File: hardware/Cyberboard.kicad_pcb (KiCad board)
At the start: 2 copper layers, 51 x 21 mm, 66 parts, among them CN1 B2B-XH-A (LF)(SN), J1 Conn_01x20, J2 Conn_01x20, SW1 SW_Push, SW2 SW_Push, U1 TPS630701RNMR, U2 NX2012SA-32.768KHZ-STD-MUB-2, U3 XL-1005UBC_C22355736, U4 STM32WB55RGVx, U5 BQ24074RGT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

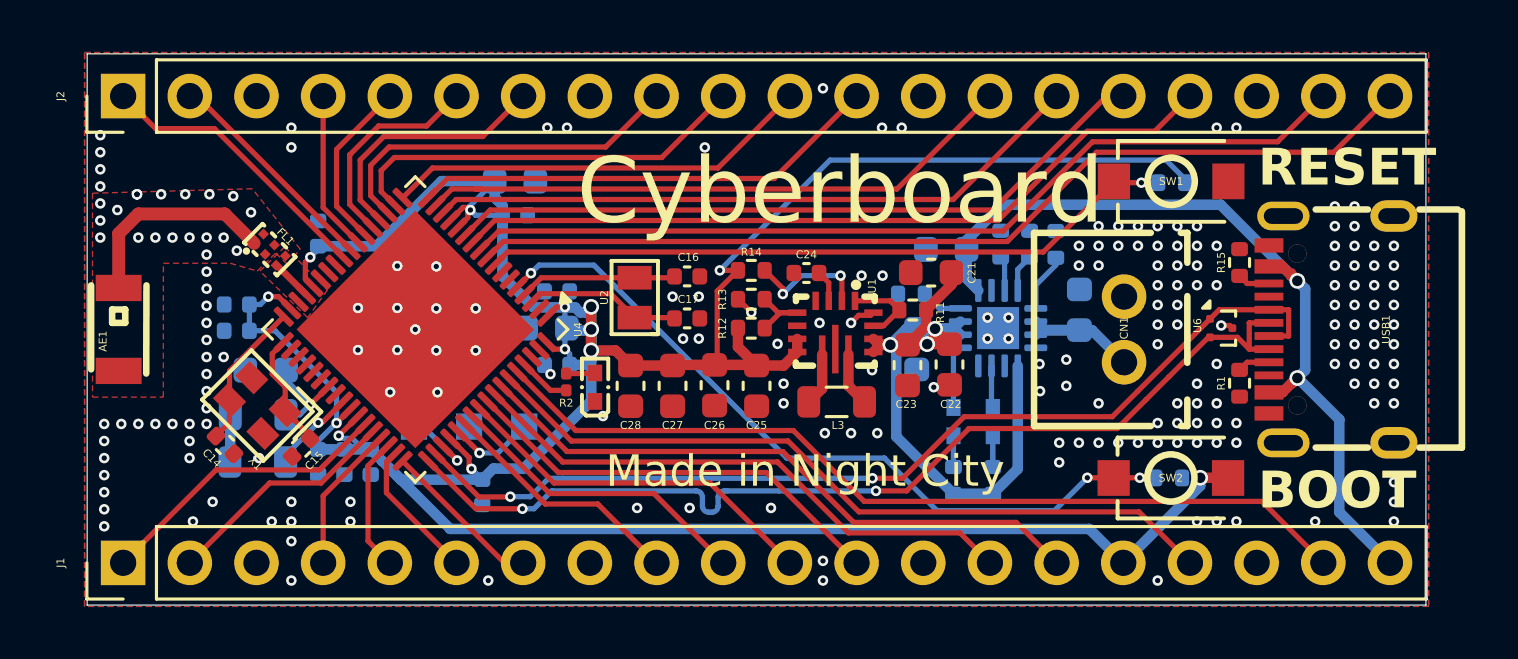
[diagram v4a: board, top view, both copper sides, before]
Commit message: updated pcb for single side pcba
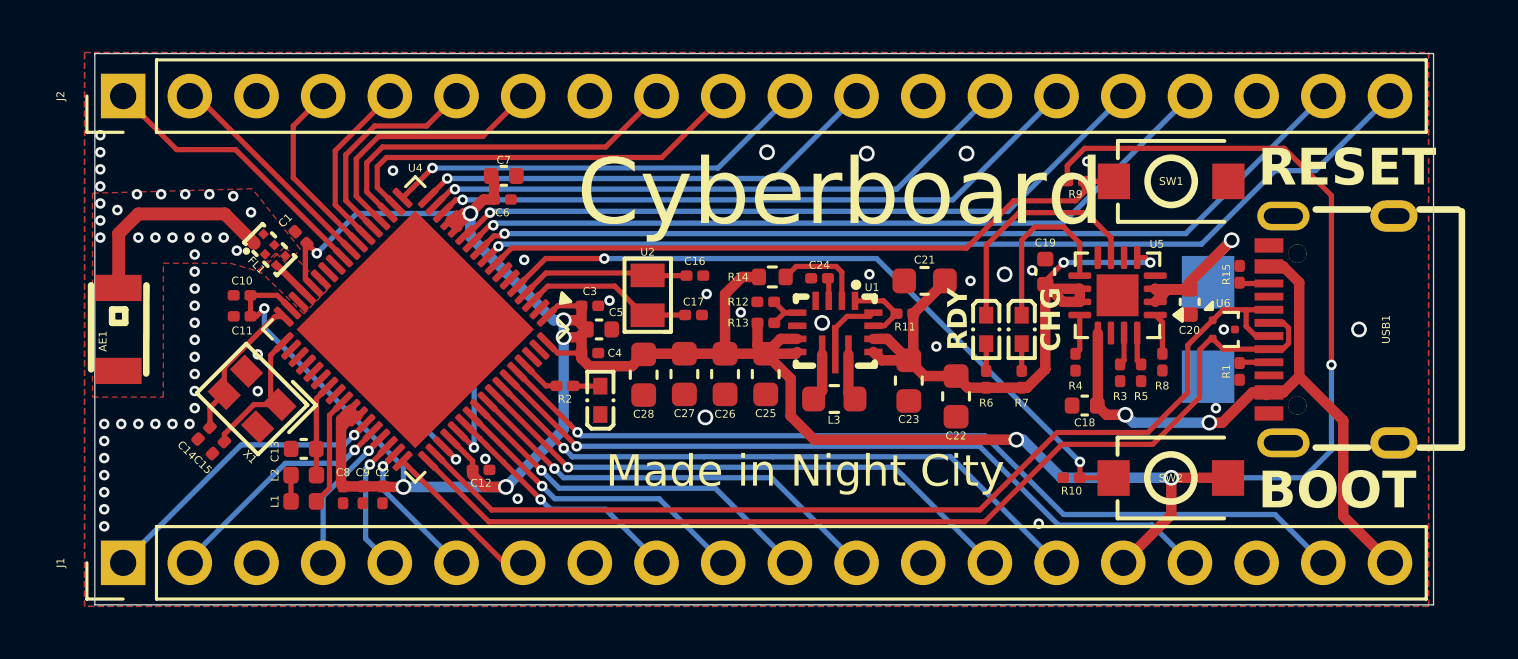
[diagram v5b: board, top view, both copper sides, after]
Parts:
- removed CN1: B2B-XH-A (LF)(SN), lcsc:CONN-TH_B2B-XH-A-LF-SN
- added TP4: TestPoint, TestPoint:TestPoint_Pad_2.0x2.0mm, B.Cu at (163.4, 76.2)
- added TP5: TestPoint, TestPoint:TestPoint_Pad_2.0x2.0mm, B.Cu at (163.4, 79.8)
- C1, C10, C11, C12, C2, C3, C4, C6, C8, C9: footprint Capacitor_SMD:C_0402_1005Metric -> Capacitor_SMD:C_0201_0603Metric; moved to F.Cu
- C13, C18, C19, C20, C5, C7: footprint Capacitor_SMD:C_0603_1608Metric -> Capacitor_SMD:C_0402_1005Metric; moved to F.Cu
- C14, C15, C16, C17, C24: footprint Capacitor_SMD:C_0402_1005Metric -> Capacitor_SMD:C_0201_0603Metric
- L1, L2: footprint Inductor_SMD:L_0805_2012Metric -> Inductor_SMD:L_0402_1005Metric; moved to F.Cu
- L3: footprint Inductor_SMD:L_0805_2012Metric -> Inductor_SMD:L_0603_1608Metric
- LED1, U3, U5: moved to F.Cu
- R1, R11, R12, R13, R15: footprint Resistor_SMD:R_0402_1005Metric -> Resistor_SMD:R_0201_0603Metric
- R10, R3, R4, R5, R6, R7, R8, R9: footprint Resistor_SMD:R_0402_1005Metric -> Resistor_SMD:R_0201_0603Metric; moved to F.Cu
- moved C18 7.95 mm to (158.8, 80.9)
- moved TP2 7.17 mm to (133.2, 75.9), turned to -90 degrees
- moved R4 6.77 mm to (158.4, 79.2), turned to 90 degrees
- moved R3 6.69 mm to (160.1, 79.7), turned to 90 degrees
- moved R5 6.49 mm to (160.9, 79.7), turned to 90 degrees
- moved R8 6.05 mm to (161.7, 79.2), turned to -90 degrees
- moved C19 5.72 mm to (157.2, 75.8), turned to 90 degrees
- moved U5 4.72 mm to (160.0, 76.7)
- moved R7 4.65 mm to (156.3, 79.9)
- moved U3 4.37 mm to (156.3, 78.0)
- moved TP3 4.27 mm to (133.2, 78.0), turned to -90 degrees
- moved C20 4.21 mm to (162.8, 77.0), turned to -90 degrees
- moved R6 3.86 mm to (155.0, 79.9)
- moved R10 3.70 mm to (158.2, 83.7), turned to 0 degrees
- moved R9 3.66 mm to (158.4, 72.3), turned to 0 degrees
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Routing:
- net +3.3V: track 133.0 -> 125.4 mm, vias 13 -> 10
- net Net-(LED1-K): track 1.60 -> 9.08 mm
- net VBUS: track 31.7 -> 25.1 mm
- net /SWCLK: track 3.30 -> 8.44 mm
- net VCC: track 29.2 -> 24.4 mm, vias 3 -> 2
- net Net-(U3-K): track 2.38 -> 6.77 mm
- net /BOOT: track 29.1 -> 27.0 mm, vias 3 -> 2
- net Net-(C20-Pad1): track 5.74 -> 7.72 mm, vias 0 -> 1
- net /RESET: track 26.7 -> 25.2 mm, vias 1 -> 0
- net /SWDIO: track 2.97 -> 4.24 mm
- net Net-(U1-PG): track 4.66 -> 3.49 mm, vias 2 -> 0
- net /HXIN: track 4.45 -> 5.60 mm
- net /GPIO13: track 6.13 -> 7.07 mm
- net Net-(U4-VLXSMPS): track 3.30 -> 4.22 mm, vias 1 -> 0
- net Net-(U1-FB): track 2.94 -> 2.09 mm
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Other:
- board text added: "+"
- board text added: "-"
- board text added: "CHG"
- board text added: "RDY"
- board text added: "[KEEP OUT]"
- board text removed: "CHGING"
- board text removed: "READY"

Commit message: prod final
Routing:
- net /SWCLK: track 8.44 -> 9.11 mm
- net GND: vias 67 -> 87

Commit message: forgot resistor values and change in inductor footprint
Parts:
- removed L3: 1.5uH, Inductor_SMD:L_0603_1608Metric
- added U8: FTC252012S1R5MBCA, lcsc:IND-SMD_L2.5-W2.0_MEKK2520TR47M, F.Cu at (149.2, 80.8)
- R12: value 470 -> 470K
- R13: value 150 -> 150K
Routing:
- net +3.3V: track 125.4 -> 124.6 mm
